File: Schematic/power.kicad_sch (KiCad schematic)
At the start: 21 parts, among them J3 Conn_01x03_Pin, U2 LM2678S-12, U5 LD1117S33TR_SOT223

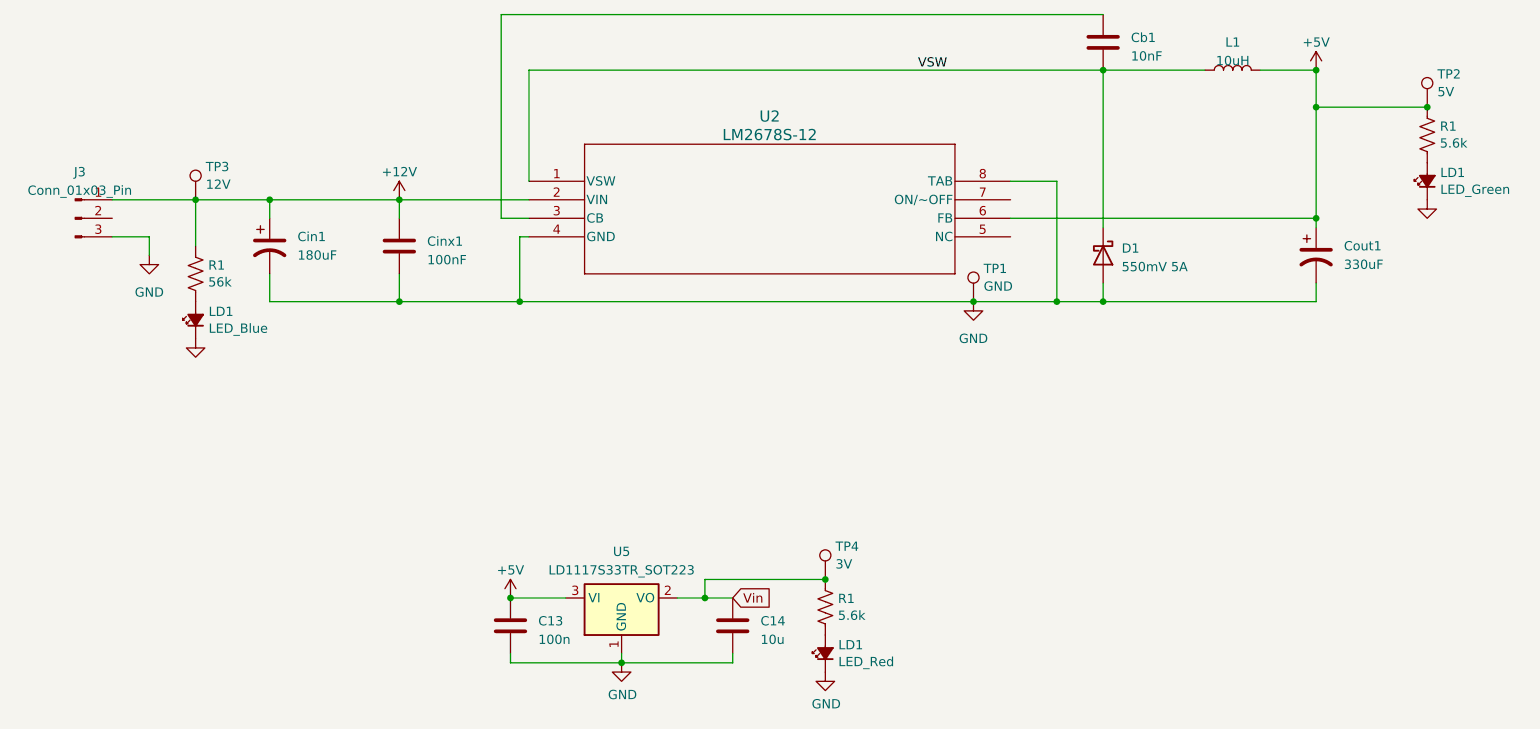
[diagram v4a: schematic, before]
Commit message: relabeld all of the components so they have more resonable numbers
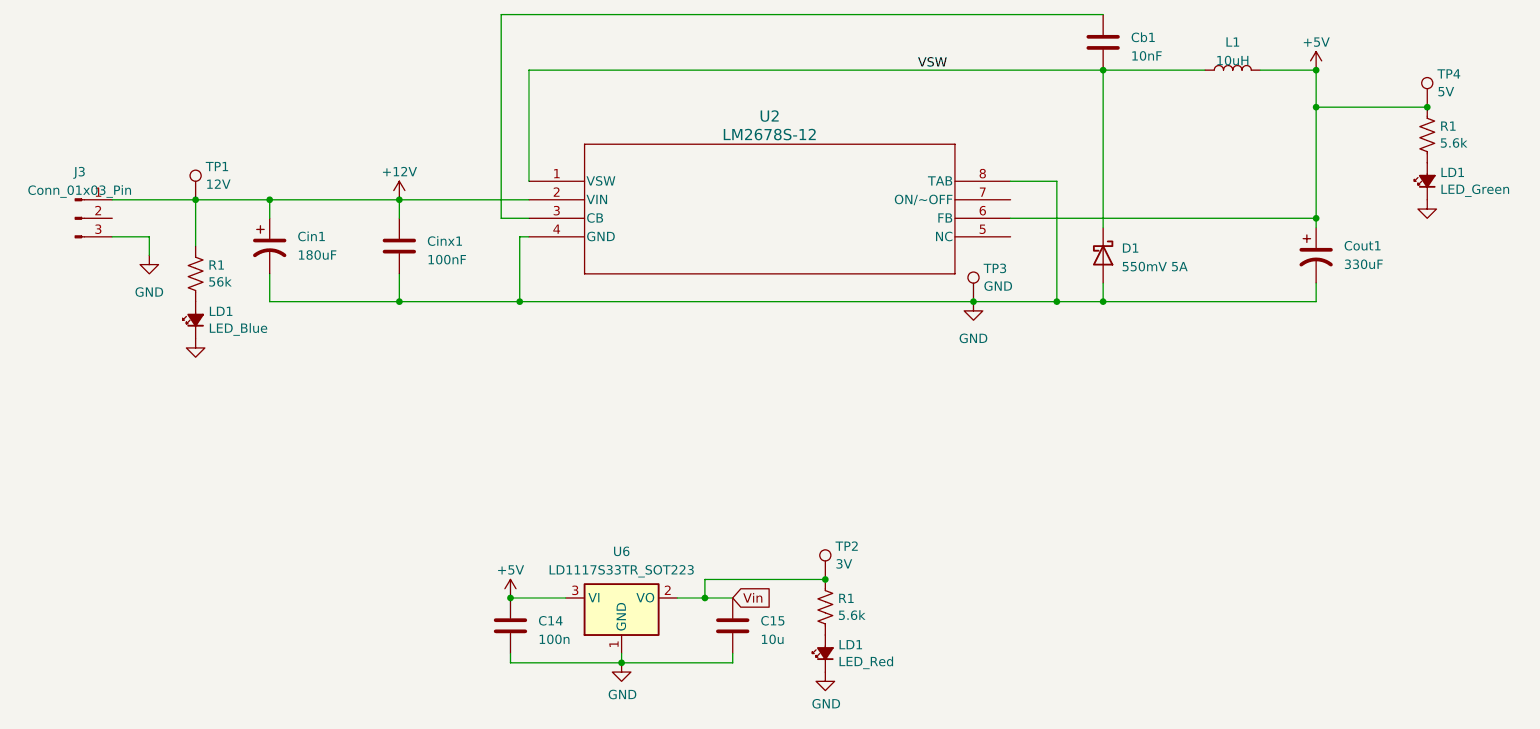
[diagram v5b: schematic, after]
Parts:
- renumbered C13 to C14, C14 to C15, TP3 to TP1, TP4 to TP2, TP1 to TP3, TP2 to TP4, U5 to U6
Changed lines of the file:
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@@
         )
         (path "/ced54cd9-3b34-40e4-aa66-964aaab81b0a/17b7dae5-2f82-4d17-9b49-7ea60414647f"
-          (reference "#PWR023") (unit 1)
+          (reference "#PWR051") (unit 1)
         )
       )
@@
       (project "Schematic"
         (path "/ced54cd9-3b34-40e4-aa66-964aaab81b0a/17b7dae5-2f82-4d17-9b49-7ea60414647f"
-          (reference "D2") (unit 1)
+          (reference "D1") (unit 1)
         )
       )
@@
   (symbol (lib_id "Connector:TestPoint") (at 138.43 96.52 0) (unit 1)
     (in_bom yes) (on_board yes) (dnp no) (fields_autoplaced)
-    (property "Reference" "TP4" (at 139.827 92.0059 0)
+    (property "Reference" "TP2" (at 139.827 92.0059 0)
       (effects (font (size 1.27 1.27)) (justify left))
     )
@@
       (project "Schematic"
         (path "/ced54cd9-3b34-40e4-aa66-964aaab81b0a/17b7dae5-2f82-4d17-9b49-7ea60414647f"
-          (reference "TP4") (unit 1)
+          (reference "TP2") (unit 1)
         )
       )
@@
         )
         (path "/ced54cd9-3b34-40e4-aa66-964aaab81b0a/17b7dae5-2f82-4d17-9b49-7ea60414647f"
-          (reference "R42") (unit 1)
+          (reference "R47") (unit 1)
         )
       )
@@
   (symbol (lib_id "Device:C") (at 95.25 102.87 0) (unit 1)
     (in_bom yes) (on_board yes) (dnp no) (fields_autoplaced)
-    (property "Reference" "C13" (at 99.06 102.235 0)
+    (property "Reference" "C14" (at 99.06 102.235 0)
       (effects (font (size 1.27 1.27)) (justify left))
     )
@@
       (project "Schematic"
         (path "/ced54cd9-3b34-40e4-aa66-964aaab81b0a/17b7dae5-2f82-4d17-9b49-7ea60414647f"
-          (reference "C13") (unit 1)
+          (reference "C14") (unit 1)
         )
       )
@@
   (symbol (lib_id "power:+5V") (at 205.74 26.67 0) (unit 1)
     (in_bom yes) (on_board yes) (dnp no) (fields_autoplaced)
-    (property "Reference" "#PWR043" (at 205.74 30.48 0)
+    (property "Reference" "#PWR054" (at 205.74 30.48 0)
       (effects (font (size 1.27 1.27)) hide)
     )
@@
       (project "Schematic"
         (path "/ced54cd9-3b34-40e4-aa66-964aaab81b0a/17b7dae5-2f82-4d17-9b49-7ea60414647f"
-          (reference "#PWR043") (unit 1)
+          (reference "#PWR054") (unit 1)
         )
       )
@@
       (project "Schematic"
         (path "/ced54cd9-3b34-40e4-aa66-964aaab81b0a/17b7dae5-2f82-4d17-9b49-7ea60414647f"
-          (reference "#PWR037") (unit 1)
+          (reference "#PWR053") (unit 1)
         )
       )
@@
         )
         (path "/ced54cd9-3b34-40e4-aa66-964aaab81b0a/17b7dae5-2f82-4d17-9b49-7ea60414647f"
-          (reference "#PWR025") (unit 1)
+          (reference "#PWR052") (unit 1)
         )
       )
@@
         )
         (path "/ced54cd9-3b34-40e4-aa66-964aaab81b0a/17b7dae5-2f82-4d17-9b49-7ea60414647f"
-          (reference "LD4") (unit 1)
+          (reference "LD5") (unit 1)
         )
       )
@@
   (symbol (lib_id "Device:C") (at 125.73 102.87 0) (unit 1)
     (in_bom yes) (on_board yes) (dnp no) (fields_autoplaced)
-    (property "Reference" "C14" (at 129.54 102.235 0)
+    (property "Reference" "C15" (at 129.54 102.235 0)
       (effects (font (size 1.27 1.27)) (justify left))
     )
@@
       (project "Schematic"
         (path "/ced54cd9-3b34-40e4-aa66-964aaab81b0a/17b7dae5-2f82-4d17-9b49-7ea60414647f"
-          (reference "C14") (unit 1)
+          (reference "C15") (unit 1)
         )
       )
@@
         )
         (path "/ced54cd9-3b34-40e4-aa66-964aaab81b0a/17b7dae5-2f82-4d17-9b49-7ea60414647f"
-          (reference "LD5") (unit 1)
+          (reference "LD4") (unit 1)
         )
       )
@@
         )
         (path "/ced54cd9-3b34-40e4-aa66-964aaab81b0a/17b7dae5-2f82-4d17-9b49-7ea60414647f"
-          (reference "#PWR045") (unit 1)
+          (reference "#PWR048") (unit 1)
         )
       )
@@
       (project "Schematic"
         (path "/ced54cd9-3b34-40e4-aa66-964aaab81b0a/17b7dae5-2f82-4d17-9b49-7ea60414647f"
-          (reference "J6") (unit 1)
+          (reference "J7") (unit 1)
         )
       )
@@
       (project "Schematic"
         (path "/ced54cd9-3b34-40e4-aa66-964aaab81b0a/17b7dae5-2f82-4d17-9b49-7ea60414647f"
-          (reference "U4") (unit 1)
+          (reference "U5") (unit 1)
         )
       )
@@
         )
         (path "/ced54cd9-3b34-40e4-aa66-964aaab81b0a/17b7dae5-2f82-4d17-9b49-7ea60414647f"
-          (reference "#PWR046") (unit 1)
+          (reference "#PWR055") (unit 1)
         )
       )
@@
   (symbol (lib_id "Connector:TestPoint") (at 220.98 31.75 0) (unit 1)
     (in_bom yes) (on_board yes) (dnp no) (fields_autoplaced)
-    (property "Reference" "TP2" (at 222.377 27.2359 0)
+    (property "Reference" "TP4" (at 222.377 27.2359 0)
       (effects (font (size 1.27 1.27)) (justify left))
     )
@@
       (project "Schematic"
         (path "/ced54cd9-3b34-40e4-aa66-964aaab81b0a/17b7dae5-2f82-4d17-9b49-7ea60414647f"
-          (reference "TP2") (unit 1)
+          (reference "TP4") (unit 1)
         )
       )
@@
   (symbol (lib_id "Connector:TestPoint") (at 52.07 44.45 0) (unit 1)
     (in_bom yes) (on_board yes) (dnp no) (fields_autoplaced)
-    (property "Reference" "TP3" (at 53.467 39.9359 0)
+    (property "Reference" "TP1" (at 53.467 39.9359 0)
       (effects (font (size 1.27 1.27)) (justify left))
     )
@@
       (project "Schematic"
         (path "/ced54cd9-3b34-40e4-aa66-964aaab81b0a/17b7dae5-2f82-4d17-9b49-7ea60414647f"
+          (reference "TP1") (unit 1)
+        )
+      )
+    )
+  )
+  (symbol (lib_id "Connector:TestPoint") (at 158.75 58.42 0) (unit 1)
+    (in_bom yes) (on_board yes) (dnp no) (fields_autoplaced)
+    (property "Reference" "TP3" (at 160.147 53.9059 0)
+      (effects (font (size 1.27 1.27)) (justify left))
+    )
+    (property "Value" "GND" (at 160.147 56.3301 0)
+      (effects (font (size 1.27 1.27)) (justify left))
+    )
+    (property "Footprint" "TestPoint:TestPoint_THTPad_D2.0mm_Drill1.0mm" (at 163.83 58.42 0)
+      (effects (font (size 1.27 1.27)) hide)
+    )
+    (property "Datasheet" "~" (at 163.83 58.42 0)
+      (effects (font (size 1.27 1.27)) hide)
+    )
+    (pin "1")
+    (instances
+      (project "Schematic"
+        (path "/ced54cd9-3b34-40e4-aa66-964aaab81b0a/17b7dae5-2f82-4d17-9b49-7ea60414647f"
           (reference "TP3") (unit 1)
         )
@@
     )
   )
-  (symbol (lib_id "Connector:TestPoint") (at 158.75 58.42 0) (unit 1)
-    (in_bom yes) (on_board yes) (dnp no) (fields_autoplaced)
-    (property "Reference" "TP1" (at 160.147 53.9059 0)
-      (effects (font (size 1.27 1.27)) (justify left))
-    )
-    (property "Value" "GND" (at 160.147 56.3301 0)
-      (effects (font (size 1.27 1.27)) (justify left))
-    )
-    (property "Footprint" "TestPoint:TestPoint_THTPad_D2.0mm_Drill1.0mm" (at 163.83 58.42 0)
-      (effects (font (size 1.27 1.27)) hide)
-    )
-    (property "Datasheet" "~" (at 163.83 58.42 0)
-      (effects (font (size 1.27 1.27)) hide)
-    )
-    (pin "1")
-    (instances
-      (project "Schematic"
-        (path "/ced54cd9-3b34-40e4-aa66-964aaab81b0a/17b7dae5-2f82-4d17-9b49-7ea60414647f"
-          (reference "TP1") (unit 1)
-        )
-      )
-    )
-  )
   (symbol (lib_id "power:+12V") (at 80.01 44.45 0) (unit 1)
     (in_bom yes) (on_board yes) (dnp no) (fields_autoplaced)
-    (property "Reference" "#PWR042" (at 80.01 48.26 0)
+    (property "Reference" "#PWR049" (at 80.01 48.26 0)
       (effects (font (size 1.27 1.27)) hide)
     )
@@
       (project "Schematic"
         (path "/ced54cd9-3b34-40e4-aa66-964aaab81b0a/17b7dae5-2f82-4d17-9b49-7ea60414647f"
-          (reference "#PWR042") (unit 1)
+          (reference "#PWR049") (unit 1)
         )
       )
@@
   (symbol (lib_id "Regulator_Linear:LD1117S33TR_SOT223") (at 110.49 99.06 0) (unit 1)
     (in_bom yes) (on_board yes) (dnp no) (fields_autoplaced)
-    (property "Reference" "U5" (at 110.49 92.71 0)
+    (property "Reference" "U6" (at 110.49 92.71 0)
       (effects (font (size 1.27 1.27)))
     )
@@
       (project "Schematic"
         (path "/ced54cd9-3b34-40e4-aa66-964aaab81b0a/17b7dae5-2f82-4d17-9b49-7ea60414647f"
-          (reference "U5") (unit 1)
+          (reference "U6") (unit 1)
         )
       )
@@
   (symbol (lib_id "power:+5V") (at 95.25 99.06 0) (unit 1)
     (in_bom yes) (on_board yes) (dnp no) (fields_autoplaced)
-    (property "Reference" "#PWR044" (at 95.25 102.87 0)
+    (property "Reference" "#PWR050" (at 95.25 102.87 0)
       (effects (font (size 1.27 1.27)) hide)
     )
@@
       (project "Schematic"
         (path "/ced54cd9-3b34-40e4-aa66-964aaab81b0a/17b7dae5-2f82-4d17-9b49-7ea60414647f"
-          (reference "#PWR044") (unit 1)
+          (reference "#PWR050") (unit 1)
         )
       )
@@
       (project "Schematic"
         (path "/ced54cd9-3b34-40e4-aa66-964aaab81b0a/17b7dae5-2f82-4d17-9b49-7ea60414647f"
-          (reference "#PWR035") (unit 1)
+          (reference "#PWR047") (unit 1)
         )
       )
@@
         )
         (path "/ced54cd9-3b34-40e4-aa66-964aaab81b0a/17b7dae5-2f82-4d17-9b49-7ea60414647f"
-          (reference "R43") (unit 1)
+          (reference "R46") (unit 1)
         )
       )
@@
         )
         (path "/ced54cd9-3b34-40e4-aa66-964aaab81b0a/17b7dae5-2f82-4d17-9b49-7ea60414647f"
-          (reference "R41") (unit 1)
-        )
-      )
+          (reference "R45") (unit 1)
+        )
+      )
